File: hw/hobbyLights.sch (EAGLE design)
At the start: 48 parts, among them U1 MCP73831-2, U2 POWER, U3 BD48K28G, U4 ATMEGA32U4-AU, U5 TPS61222, Y1 RESONATORSMD

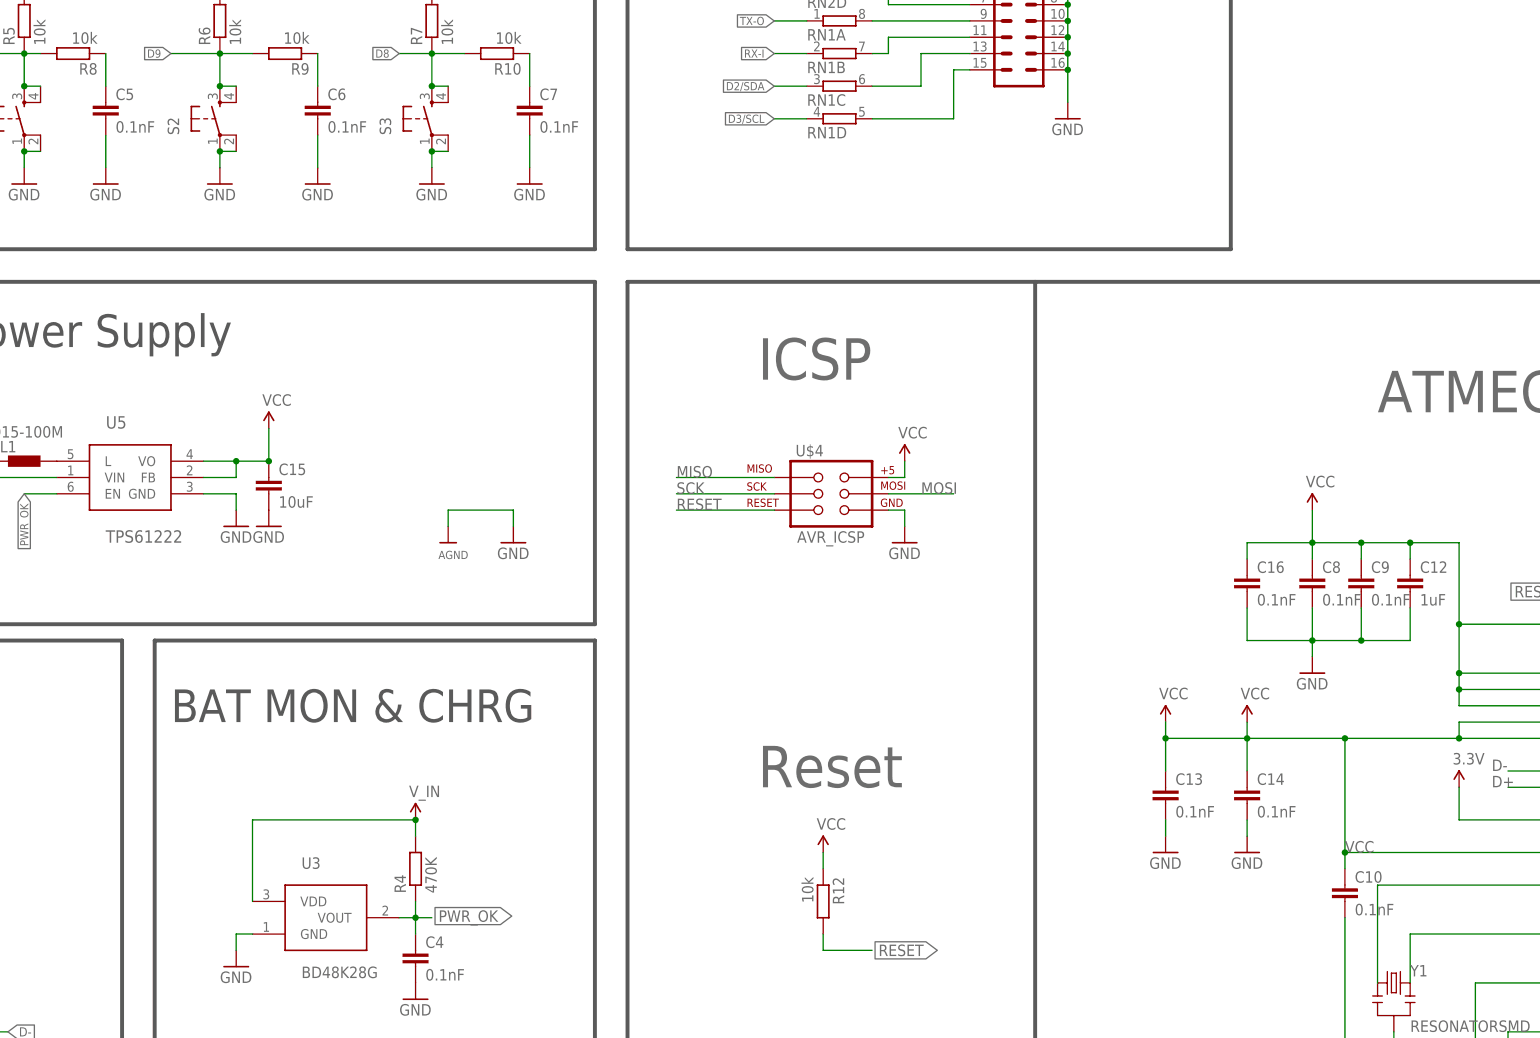
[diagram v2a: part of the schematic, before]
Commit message: Updated PCB removing daughter motor boards.
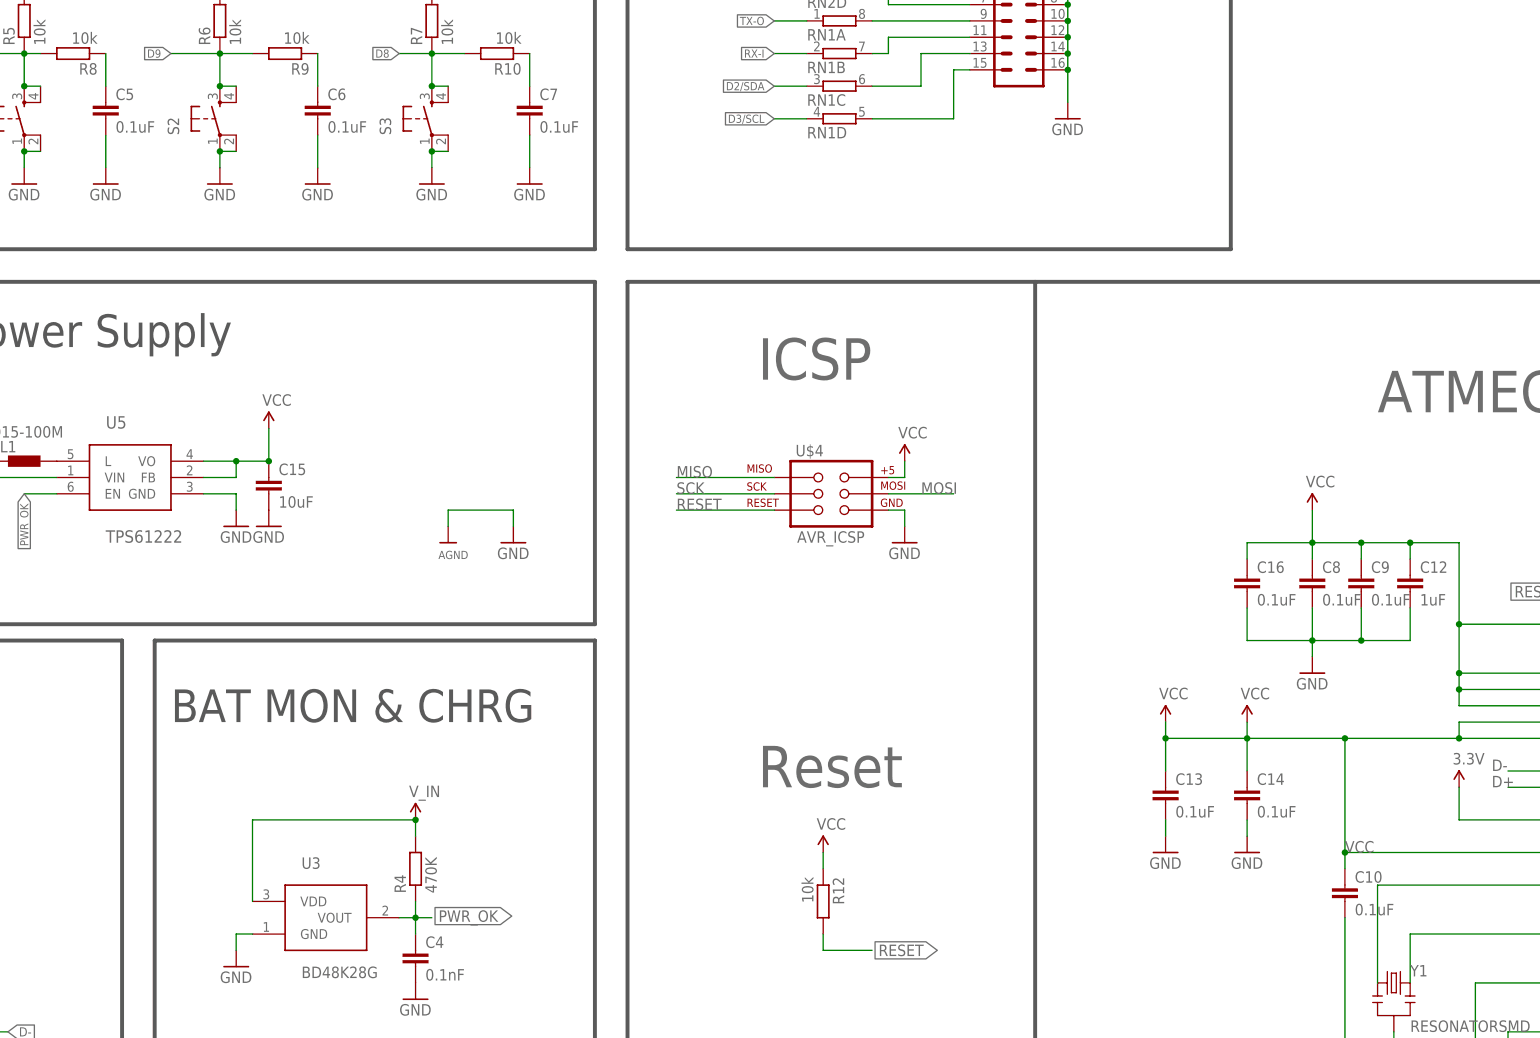
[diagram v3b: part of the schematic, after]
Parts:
- C10, C13, C14, C16, C5, C6, C7, C8, C9: value 0.1nF -> 0.1uF
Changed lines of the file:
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@@
 <?xml version="1.0" encoding="utf-8"?>
 <!DOCTYPE eagle SYSTEM "eagle.dtd">
-<eagle version="7.0.0">
+<eagle version="7.4.0">
 <drawing>
 <settings>
@@
 <part name="R9" library="rcl" deviceset="R-EU_" device="R0603" value="10k"/>
 <part name="R10" library="rcl" deviceset="R-EU_" device="R0603" value="10k"/>
-<part name="C5" library="rcl" deviceset="C-EU" device="C0603" value="0.1nF"/>
-<part name="C6" library="rcl" deviceset="C-EU" device="C0603" value="0.1nF"/>
-<part name="C7" library="rcl" deviceset="C-EU" device="C0603" value="0.1nF"/>
+<part name="C5" library="rcl" deviceset="C-EU" device="C0603" value="0.1uF"/>
+<part name="C6" library="rcl" deviceset="C-EU" device="C0603" value="0.1uF"/>
+<part name="C7" library="rcl" deviceset="C-EU" device="C0603" value="0.1uF"/>
 <part name="GND9" library="supply1" deviceset="GND" device=""/>
 <part name="GND10" library="supply1" deviceset="GND" device=""/>
@@
 <part name="FRAME1" library="frames" deviceset="DINA3_L" device=""/>
 <part name="R11" library="rcl" deviceset="R-EU_" device="R0603" value="10k"/>
-<part name="C8" library="rcl" deviceset="C-EU" device="C0603" value="0.1nF"/>
-<part name="C9" library="rcl" deviceset="C-EU" device="C0603" value="0.1nF"/>
-<part name="C10" library="rcl" deviceset="C-EU" device="C0603" value="0.1nF"/>
+<part name="C8" library="rcl" deviceset="C-EU" device="C0603" value="0.1uF"/>
+<part name="C9" library="rcl" deviceset="C-EU" device="C0603" value="0.1uF"/>
+<part name="C10" library="rcl" deviceset="C-EU" device="C0603" value="0.1uF"/>
 <part name="C12" library="rcl" deviceset="C-EU" device="C0603" value="1uF"/>
 <part name="GND24" library="SparkFun" deviceset="GND" device=""/>
@@
 <part name="S3" library="SAVMakerI" deviceset="SPARKFUN_TAC_SWITCH" device="SMD"/>
 <part name="U$4" library="fmc" deviceset="AVR_ICSP" device=""/>
-<part name="C13" library="rcl" deviceset="C-EU" device="C0603" value="0.1nF"/>
-<part name="C14" library="rcl" deviceset="C-EU" device="C0603" value="0.1nF"/>
+<part name="C13" library="rcl" deviceset="C-EU" device="C0603" value="0.1uF"/>
+<part name="C14" library="rcl" deviceset="C-EU" device="C0603" value="0.1uF"/>
 <part name="GND25" library="SparkFun" deviceset="GND" device=""/>
 <part name="GND27" library="SparkFun" deviceset="GND" device=""/>
@@
 <part name="RN1" library="resistor-dil" deviceset="4R-N" device="EXBS8V"/>
 <part name="RN2" library="resistor-dil" deviceset="4R-N" device="EXBS8V"/>
-<part name="C16" library="rcl" deviceset="C-EU" device="C0603" value="0.1nF"/>
+<part name="C16" library="rcl" deviceset="C-EU" device="C0603" value="0.1uF"/>
 <part name="D1" library="diode" deviceset="MBR0520LT" device=""/>
 <part name="SUPPLY4" library="SparkFun-Aesthetics" deviceset="V_USB" device=""/>
